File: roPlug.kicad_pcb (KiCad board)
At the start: 2 copper layers, 25 x 26 mm, 18 parts, among them P1 USB_C_Plug, SW1 Rotary_Encoder_Switch, U1 ATmega32U4-MU, Y1 16MHz

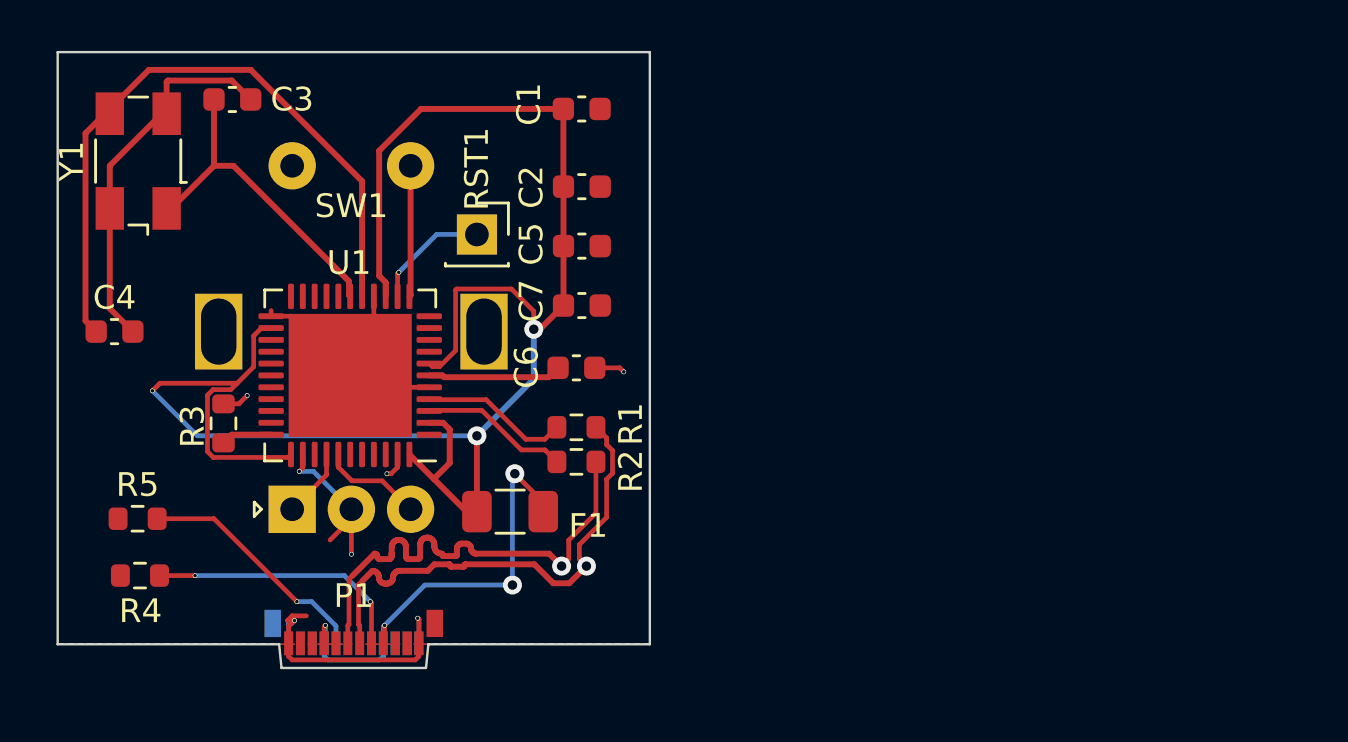
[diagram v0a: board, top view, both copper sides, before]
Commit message: change the edgecuts to be the same as the framework expansion cards
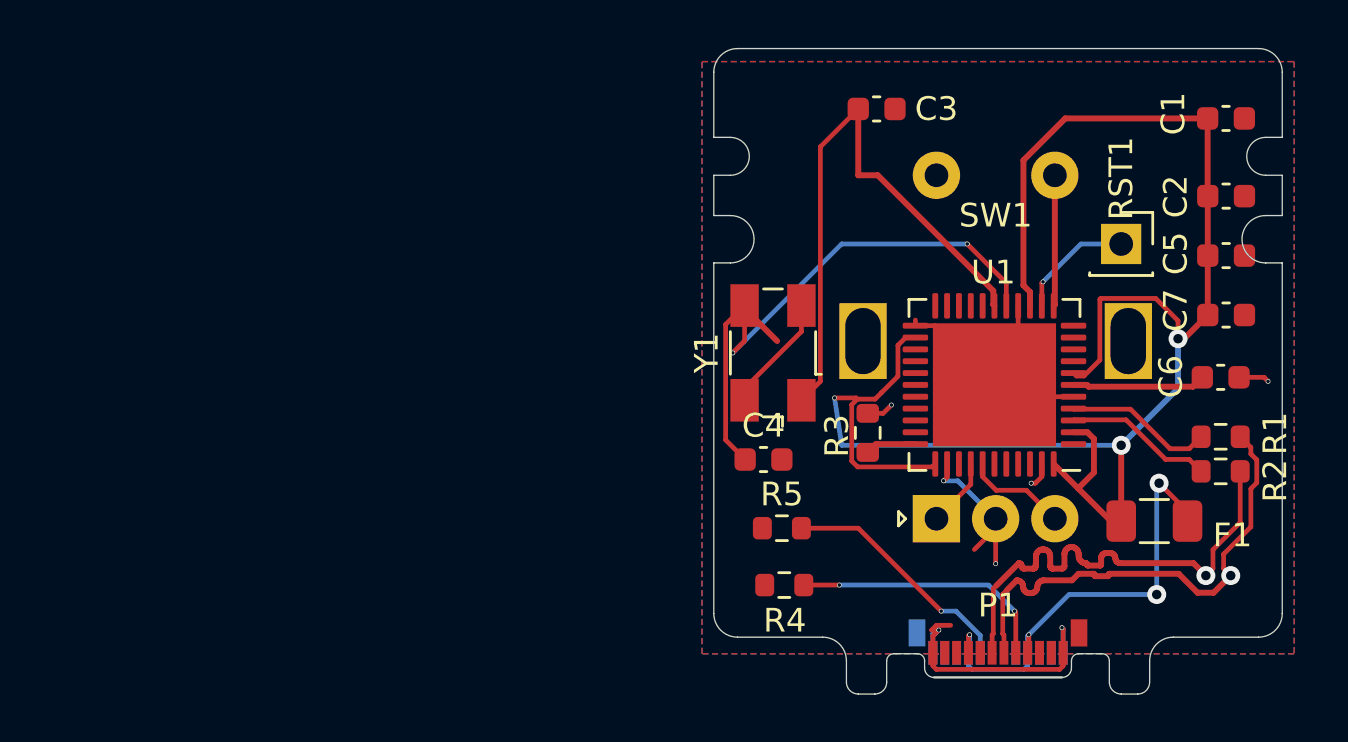
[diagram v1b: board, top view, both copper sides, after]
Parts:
- moved Y1 28.0 mm to (130.2, 62.7)
- moved C4 27.9 mm to (129.8, 67.2)
- moved C2 27.2 mm to (149.3, 56.1)
- moved C5 27.2 mm to (149.3, 58.6)
- moved C7 27.2 mm to (149.3, 61.1)
- moved F1 27.2 mm to (146.3, 69.8)
- moved R4 27.2 mm to (130.7, 72.5)
- moved U1 27.2 mm to (139.6, 64.0)
- moved RST1 27.2 mm to (144.9, 58.1)
- moved C1 27.2 mm to (149.3, 52.8)
- moved C3 27.2 mm to (134.6, 52.4)
- moved C6 27.2 mm to (149.1, 63.7)
- moved P1 27.2 mm to (139.7, 75.4)
- moved R1 27.2 mm to (149.1, 66.2)
- moved R2 27.2 mm to (149.1, 67.7)
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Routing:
- net GND: track 50.8 -> 39.9 mm
- net Net-(C3-Pad1): track 14.0 -> 24.5 mm
- net +5V: track 78.0 -> 74.6 mm
- net Net-(C4-Pad1): track 28.2 -> 25.9 mm, vias 0 -> 2
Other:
- board size 25 x 26 mm -> 24 x 27.2 mm

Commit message: fix up footprints hanging off the sides of the cut
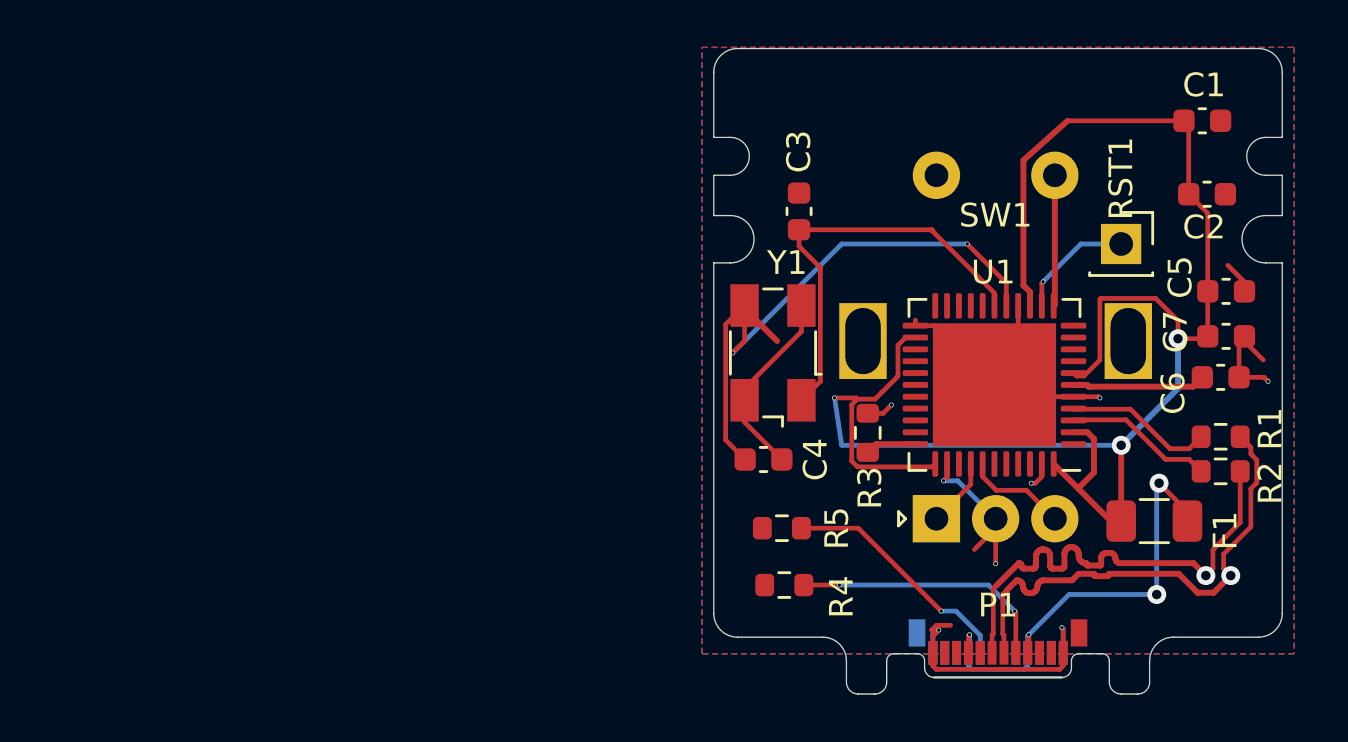
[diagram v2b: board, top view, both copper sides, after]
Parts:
- moved C3 5.43 mm to (131.3, 56.7), turned to 90 degrees
- moved C5 1.51 mm to (149.3, 60.1)
- moved C1 1.00 mm to (148.3, 52.9)
- moved C7 0.90 mm to (149.3, 62.0)
- moved C2 0.81 mm to (148.5, 56.0)
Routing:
- net GND: track 39.9 -> 49.0 mm, vias 7 -> 8
- net Net-(C3-Pad1): track 24.5 -> 17.8 mm
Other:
- board text added: "B7"
- board text added: "F5"
- board text added: "F6"
- board text added: "GND"
- board text added: "RST"

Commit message: fix pcb wiring and update readme for laternative parts
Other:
- board text added: "27 x 24 mm (LxW)"

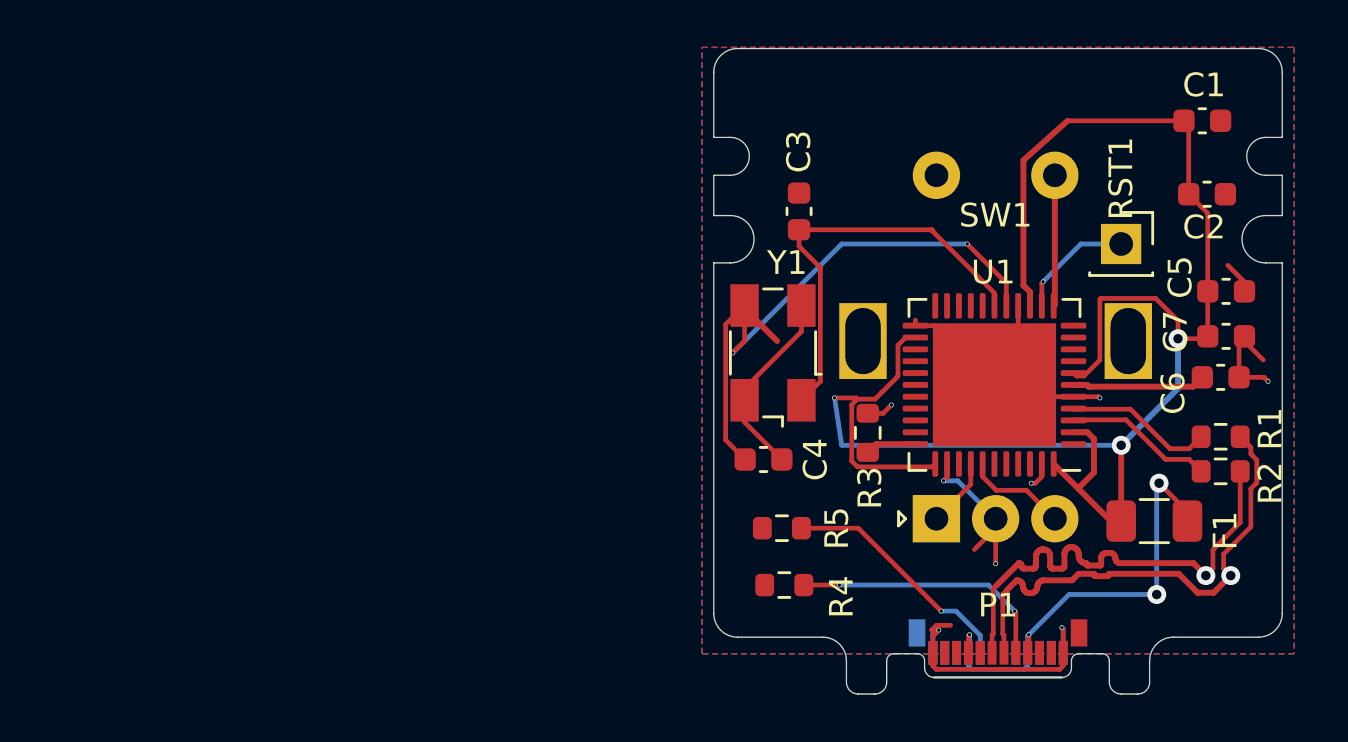
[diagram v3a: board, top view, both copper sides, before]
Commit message: remove gerber & fix capacitors bad wiring
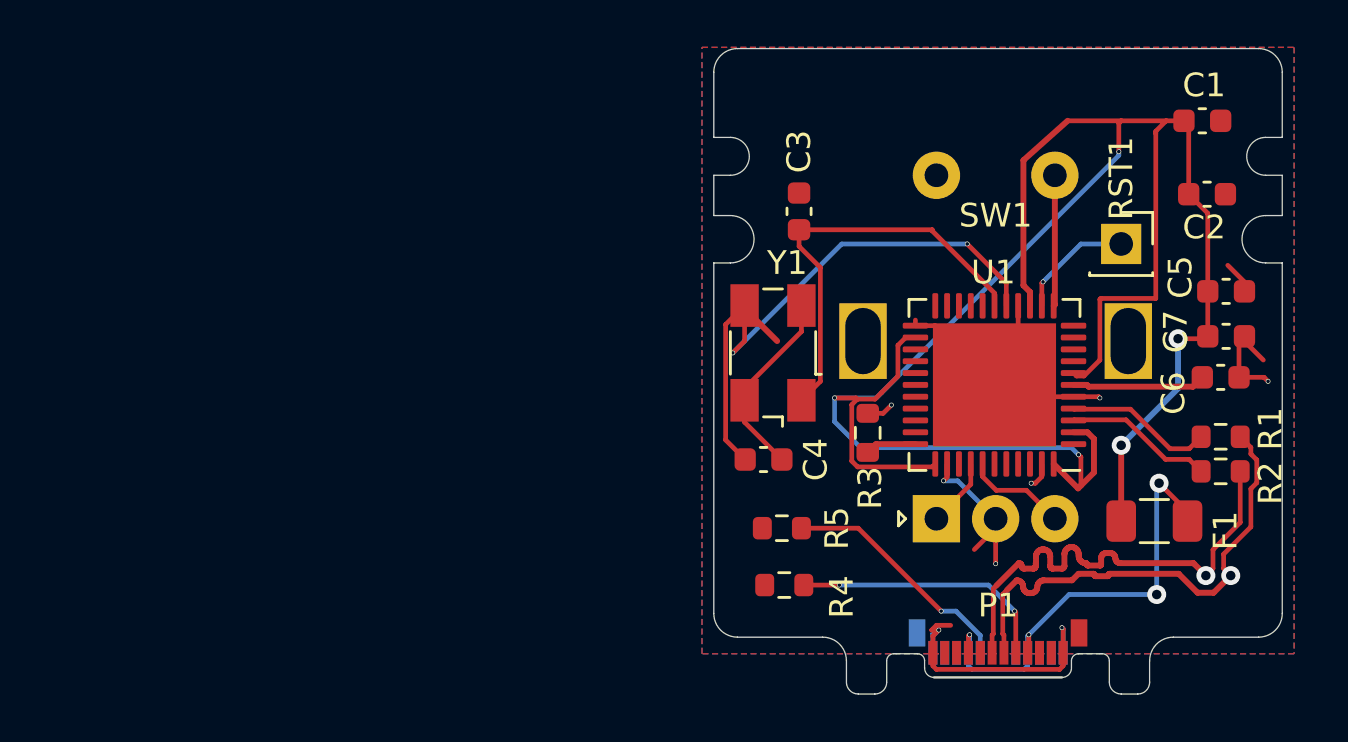
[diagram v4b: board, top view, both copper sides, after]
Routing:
- net +5V: track 74.3 -> 95.1 mm, vias 3 -> 5
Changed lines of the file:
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@@
   (general
     (thickness 0.8)
-    (drawings 57)
-    (tracks 404)
+    (drawings 58)
+    (tracks 418)
     (zones 0)
     (modules 18)
@@
       (rotate (xyz 0 0 0))
     )
+  )
+  (gr_text GND (at 139.5 67.4) (layer B.SilkS)
+    (effects (font (size 1 1) (thickness 0.15)) (justify mirror))
   )
   (gr_text "27 x 24 mm (LxW)" (at 141.9 80.3) (layer Cmts.User)
@@
   (segment (start 129 64.7) (end 129 65.625) (width 0.2) (layer F.Cu) (net 1))
   (segment (start 144.9 69.8) (end 144.4625 69.8) (width 0.25) (layer F.Cu) (net 2))
-  (segment (start 143.75001 67.74999) (end 143.08125 68.41875) (width 0.25) (layer F.Cu) (net 2))
   (segment (start 143.473022 66.05) (end 143.75001 66.326988) (width 0.25) (layer F.Cu) (net 2))
   (segment (start 142.8875 66.05) (end 143.473022 66.05) (width 0.25) (layer F.Cu) (net 2))
   (segment (start 143.75001 66.326988) (end 143.75001 67.74999) (width 0.25) (layer F.Cu) (net 2))
   (segment (start 143.08125 68.41875) (end 142.05 67.3875) (width 0.25) (layer F.Cu) (net 2))
-  (segment (start 144.4625 69.8) (end 143.08125 68.41875) (width 0.25) (layer F.Cu) (net 2))
   (via (at 144.9 66.6) (size 0.8) (drill 0.4) (layers F.Cu B.Cu) (net 2))
   (segment (start 144.9 69.8) (end 144.9 66.6) (width 0.25) (layer F.Cu) (net 2))
@@
   (segment (start 147.3 64.2) (end 147.3 62.1) (width 0.25) (layer B.Cu) (net 2))
   (segment (start 144.9 66.6) (end 147.3 64.2) (width 0.25) (layer B.Cu) (net 2))
-  (segment (start 147.3 61.339998) (end 147.3 62.1) (width 0.2) (layer F.Cu) (net 2))
-  (segment (start 146.360001 60.399999) (end 147.3 61.339998) (width 0.2) (layer F.Cu) (net 2))
-  (segment (start 144.039999 60.399999) (end 146.360001 60.399999) (width 0.2) (layer F.Cu) (net 2))
-  (segment (start 143.999999 60.439999) (end 144.039999 60.399999) (width 0.2) (layer F.Cu) (net 2))
-  (segment (start 143.999999 63.000001) (end 143.999999 60.439999) (width 0.2) (layer F.Cu) (net 2))
-  (segment (start 143.325 63.675) (end 143.999999 63.000001) (width 0.2) (layer F.Cu) (net 2))
-  (segment (start 143.0125 63.675) (end 143.325 63.675) (width 0.2) (layer F.Cu) (net 2))
-  (segment (start 142.8875 63.55) (end 143.0125 63.675) (width 0.2) (layer F.Cu) (net 2))
   (segment (start 136.925 67.5125) (end 137.05 67.3875) (width 0.2) (layer F.Cu) (net 2))
   (segment (start 133.7718 67.5125) (end 136.925 67.5125) (width 0.2) (layer F.Cu) (net 2))
@@
   (segment (start 135.47499 63.685012) (end 134.780001 64.380001) (width 0.2) (layer F.Cu) (net 2))
   (segment (start 134.780001 64.380001) (end 134.510012 64.64999) (width 0.2) (layer F.Cu) (net 2))
-  (segment (start 133.1 66.6) (end 144.9 66.6) (width 0.2) (layer B.Cu) (net 2))
-  (segment (start 132.8 64.6) (end 133.1 66.6) (width 0.2) (layer B.Cu) (net 2))
   (segment (start 133.70932 64.6) (end 133.75931 64.64999) (width 0.2) (layer F.Cu) (net 2))
   (segment (start 132.8 64.6) (end 133.70932 64.6) (width 0.2) (layer F.Cu) (net 2))
@@
   (segment (start 140.773012 54.565986) (end 140.773012 59.84999) (width 0.25) (layer F.Cu) (net 2))
   (segment (start 142.638998 52.9) (end 140.773012 54.565986) (width 0.25) (layer F.Cu) (net 2))
-  (segment (start 147.55 52.9) (end 142.638998 52.9) (width 0.2) (layer F.Cu) (net 2))
+  (segment (start 142.8875 63.55) (end 143.0125 63.675) (width 0.2) (layer F.Cu) (net 2))
+  (segment (start 143.0125 63.675) (end 143.325 63.675) (width 0.2) (layer F.Cu) (net 2))
+  (segment (start 143.325 63.675) (end 143.999999 63.000001) (width 0.2) (layer F.Cu) (net 2))
+  (segment (start 143.999999 63.000001) (end 143.999999 60.439999) (width 0.2) (layer F.Cu) (net 2))
+  (segment (start 143.999999 60.439999) (end 144.039999 60.399999) (width 0.2) (layer F.Cu) (net 2))
+  (segment (start 144.039999 60.399999) (end 146.360001 60.399999) (width 0.2) (layer F.Cu) (net 2))
+  (segment (start 146.360001 53.339999) (end 146.8 52.9) (width 0.2) (layer F.Cu) (net 2))
+  (segment (start 147.55 52.9) (end 146.8 52.9) (width 0.2) (layer F.Cu) (net 2))
+  (via (at 143.1 67) (size 0.2) (drill 0.15) (layers F.Cu B.Cu) (net 2))
+  (segment (start 143.2 67.1) (end 143.1 67) (width 0.2) (layer F.Cu) (net 2))
+  (segment (start 143.75001 67.74999) (end 143.2 68.3) (width 0.25) (layer F.Cu) (net 2))
+  (segment (start 143.2 68.3) (end 143.2 67.1) (width 0.2) (layer F.Cu) (net 2))
+  (segment (start 143.2 68.3) (end 143.08125 68.41875) (width 0.25) (layer F.Cu) (net 2))
+  (segment (start 143.1 67) (end 142.8 66.7) (width 0.2) (layer B.Cu) (net 2))
+  (segment (start 142.8 66.7) (end 133.9 66.7) (width 0.2) (layer B.Cu) (net 2))
+  (segment (start 132.8 65.6) (end 132.8 64.6) (width 0.2) (layer B.Cu) (net 2))
+  (segment (start 133.9 66.7) (end 132.8 65.6) (width 0.2) (layer B.Cu) (net 2))
+  (via (at 144.8 54.2) (size 0.2) (drill 0.15) (layers F.Cu B.Cu) (net 2))
+  (segment (start 144.8 54.360002) (end 144.8 54.2) (width 0.2) (layer B.Cu) (net 2))
+  (segment (start 134.560002 64.6) (end 144.8 54.360002) (width 0.2) (layer B.Cu) (net 2))
+  (segment (start 132.8 64.6) (end 134.560002 64.6) (width 0.2) (layer B.Cu) (net 2))
+  (segment (start 146.360001 53.439999) (end 146.360001 53.339999) (width 0.2) (layer F.Cu) (net 2))
+  (segment (start 146.360001 60.399999) (end 146.360001 53.439999) (width 0.2) (layer F.Cu) (net 2))
+  (segment (start 144.8 54.2) (end 144.8 53) (width 0.2) (layer F.Cu) (net 2))
+  (segment (start 144.8 53) (end 144.9 52.9) (width 0.2) (layer F.Cu) (net 2))
+  (segment (start 144.9 52.9) (end 142.638998 52.9) (width 0.2) (layer F.Cu) (net 2))
+  (segment (start 146.8 52.9) (end 144.9 52.9) (width 0.2) (layer F.Cu) (net 2))
   (segment (start 132.200001 63.899999) (end 131.4 64.7) (width 0.2) (layer F.Cu) (net 3))
   (segment (start 132.200001 59.100001) (end 132.200001 63.899999) (width 0.2) (layer F.Cu) (net 3))
@@
   (segment (start 129 62.2) (end 129 60.7) (width 0.2) (layer F.Cu) (net 4))
   (segment (start 128.5 62.7) (end 129 62.2) (width 0.2) (layer F.Cu) (net 4))
+  (segment (start 148.325 63.73) (end 147.929999 64.125001) (width 0.25) (layer F.Cu) (net 5))
+  (segment (start 147.929999 64.125001) (end 143.525021 64.125001) (width 0.25) (layer F.Cu) (net 5))
+  (segment (start 143.525021 64.125001) (end 143.45002 64.05) (width 0.25) (layer F.Cu) (net 5))
   (segment (start 143.45002 64.05) (end 142.8875 64.05) (width 0.25) (layer F.Cu) (net 5))
-  (segment (start 143.525021 64.125001) (end 143.45002 64.05) (width 0.25) (layer F.Cu) (net 5))
-  (segment (start 147.929999 64.125001) (end 143.525021 64.125001) (width 0.25) (layer F.Cu) (net 5))
-  (segment (start 148.325 63.73) (end 147.929999 64.125001) (width 0.25) (layer F.Cu) (net 5))
   (via (at 146.4 72.9) (size 0.8) (drill 0.4) (layers F.Cu B.Cu) (net 6))
   (segment (start 147.7 69.8) (end 147.3 69.8) (width 0.25) (layer F.Cu) (net 6))

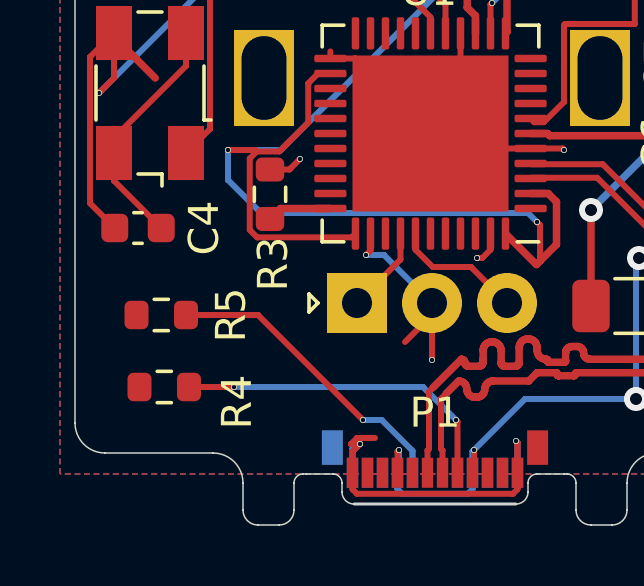
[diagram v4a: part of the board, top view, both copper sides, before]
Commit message: update schematics and fix USB-C circuitry for host detection
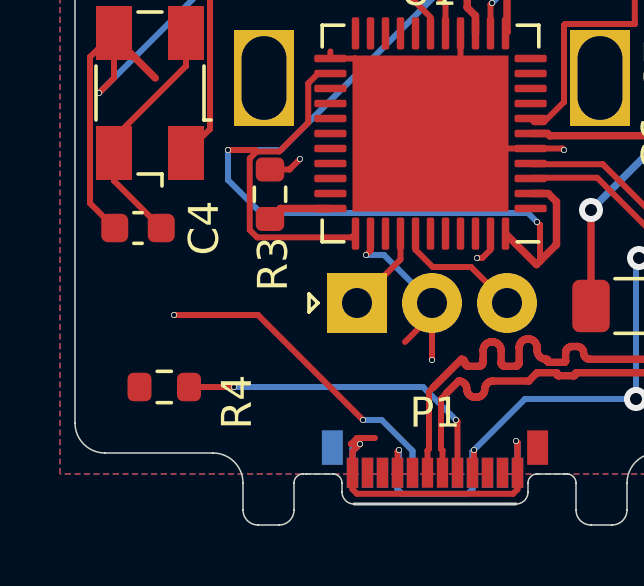
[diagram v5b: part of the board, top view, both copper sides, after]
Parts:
- removed R5: 22, Resistor_SMD:R_0603_1608Metric
- R4: value 22 -> 5.1k
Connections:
- P1 pad B5: Net-(P1-PadB5) -> (no net)
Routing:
- net (no net): track 0.00 -> 10.6 mm, vias 0 -> 2
- net Net-(P1-PadB5): track 10.2 -> 0.00 mm, vias 1 -> 0
